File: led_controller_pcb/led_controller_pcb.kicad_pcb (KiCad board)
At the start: 2 copper layers, 50.2 x 99.7 mm, 93 parts, among them J1 DCDC, J10 PASSIVE_OUT, J11 VPP, J12 OUT, J13 VPP, J14 OUT, J15 VPP, J16 PASSIVE_OUT, J17 VPP, J18 OUT, J19 VPP, J2 DEBUG, J20 OUT, J21 LINE1_IN, J22 LINE2_IN, J24 HV_LINE, J25 HV_OUT, J26 HV_LINE, J27 HV_OUT, J28 PSU_LINE1, J29 PSU_LINE2, J3 VPP, J31 PSU_GND, J32 PSU_VOUT, J4 PASSIVE_OUT, J5 VPP, J6 OUT, J7 VPP, J8 OUT, J9 VPP, Q1 IRF540N, Q10 BT136-600, Q2 IRF540N, Q3 IRF540N, Q4 IRF540N, Q5 IRF540N, Q6 IRF540N, Q7 BC549, Q8 BC549, Q9 BT136-600, SW1 BUTTON, SW2 BUTTON, U1 ESP-12E, U2 TC4427A, U3 TC4427A, U4 TC4427A, U5 STM32F030F4Px, U6 MOC3023M, U7 MOC3023M, U8 H11AA1, Y1 8MHz

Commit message: fix tim1 pwm
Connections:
- J2 pad 10: /TX_SCL -> /TX
- J2 pad 8: /RX_SDA -> /RX
- R11 pad 1: /TIM15_CH2 -> /TIM1_CH3
- R7 pad 1: /TIM15_CH1 -> /TIM1_CH2
- U2 pad 2: /TIM15_CH1 -> /TIM1_CH2
- U3 pad 4: /TIM15_CH2 -> /TIM1_CH3
- U5 pad 17: /TX_SCL -> /TIM1_CH2
- U5 pad 18: /RX_SDA -> /TIM1_CH3
- U5 pad 8: /TIM15_CH1 -> /TX
- U5 pad 9: /TIM15_CH2 -> /RX
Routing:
- net /TX: vias 0 -> 2
- net /TIM15_CH1: vias 2 -> 0

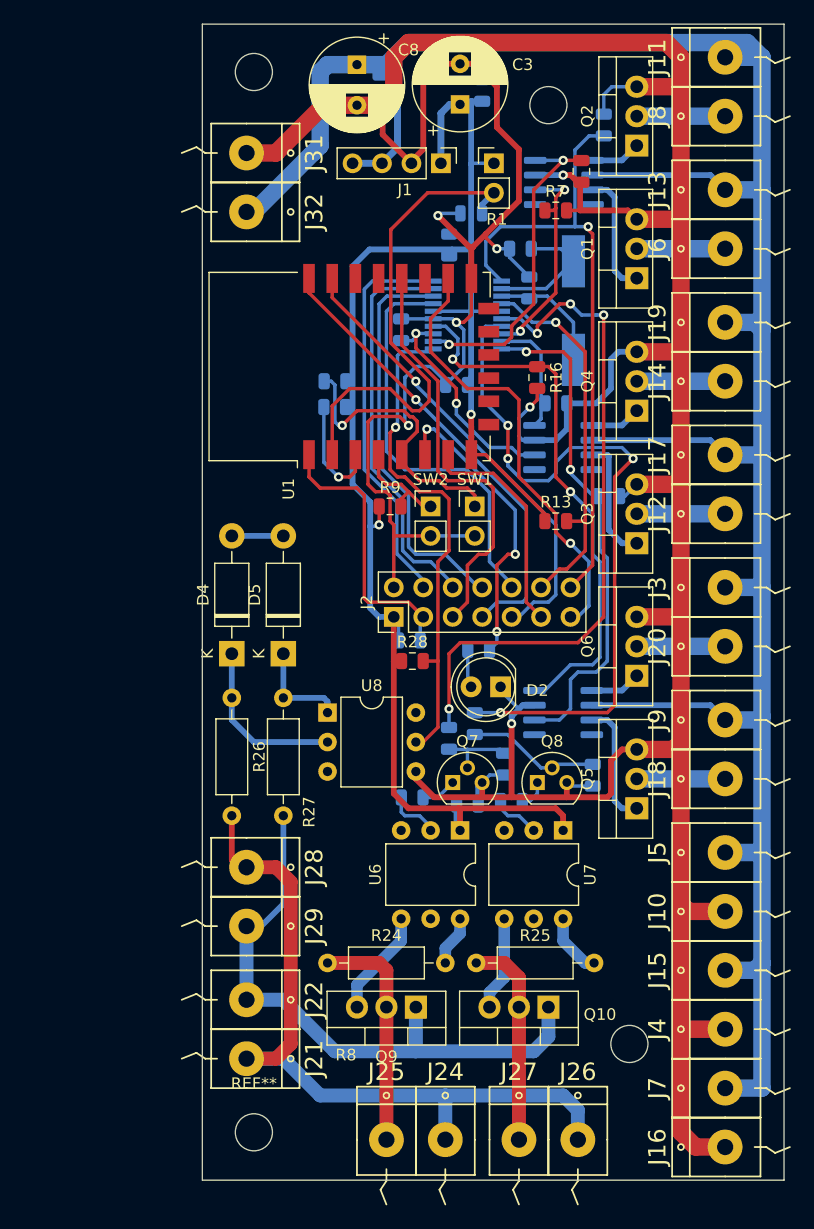
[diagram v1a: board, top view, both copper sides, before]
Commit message: reroute traces to use other timer
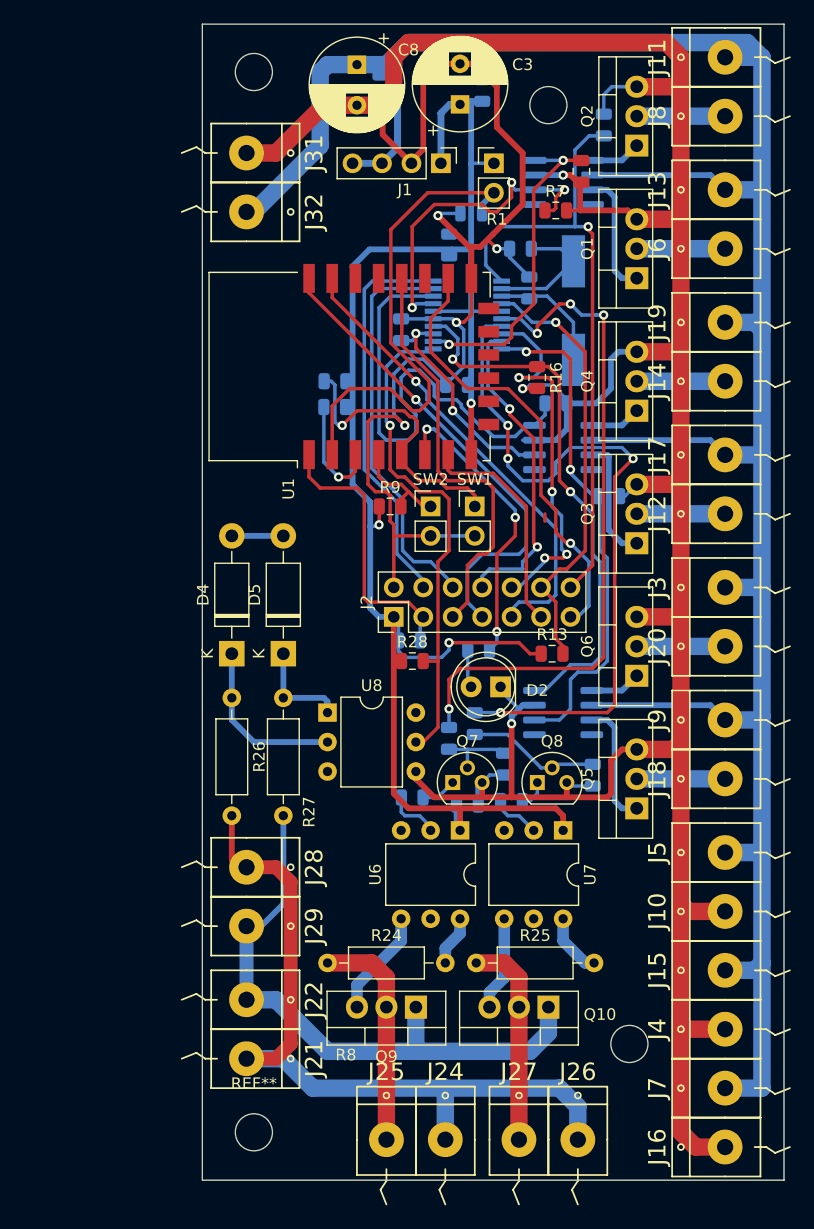
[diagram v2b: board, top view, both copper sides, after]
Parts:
- moved R13 11.4 mm to (147.6, 106.7)
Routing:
- net /TIM1_CH3: track 0.00 -> 42.3 mm
- net /TX_SCL: track 35.7 -> 0.00 mm
- net /RX_SDA: track 34.8 -> 0.00 mm
- net /TX: track 0.00 -> 32.7 mm, vias 2 -> 4
- net /TIM1_CH2: track 0.00 -> 28.4 mm, vias 0 -> 3
- net /RX: track 0.00 -> 28.0 mm, vias 0 -> 2
- net /TIM15_CH1: track 19.1 -> 0.00 mm
- net /TIM15_CH2: track 11.1 -> 0.00 mm
- net +3V3: track 141.4 -> 147.7 mm, vias 2 -> 3
- net /RST: track 32.8 -> 37.7 mm
- net GND: track 368.4 -> 370.9 mm
- net /ESP_TX: track 39.8 -> 41.4 mm
- net /LINE1: track 65.6 -> 66.5 mm
- net /GPO1: track 58.2 -> 58.9 mm
- net /ESP_RX: track 39.9 -> 40.6 mm

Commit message: finalise PCB
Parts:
- added C10: 10p, Capacitor_SMD:C_0805_2012Metric, F.Cu at (135.6, 69.5)
- added R5: 4.7k, Resistor_SMD:R_0805_2012Metric, B.Cu at (137.2, 107.0)
- R13: moved to B.Cu
- moved R9 1.92 mm to (131.7, 94.0)
- moved J2 1.91 mm to (132.1, 103.5)
- moved R3 1.90 mm to (133.4, 105.5)
- moved R13 0.71 mm to (147.0, 106.4)
- moved R28 0.32 mm to (135.9, 107.3)
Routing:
- net /ESP_GP0: track 36.2 -> 40.7 mm
- net /RST: track 37.7 -> 40.2 mm
- net /ESP_RST: track 24.1 -> 21.9 mm
- net GND: track 370.9 -> 373.0 mm
- net /BOOT0: track 55.4 -> 57.3 mm
- net /TIM3_CH4: track 46.8 -> 44.9 mm
- net /SWDIO: track 34.4 -> 32.8 mm
- net Net-(C10-Pad1): track 42.9 -> 41.4 mm
- net /TIM14_CH1: track 43.5 -> 42.1 mm
- net /RX: track 28.0 -> 26.6 mm
- net VDD: track 220.9 -> 219.9 mm
- net /TIM1_CH2: track 28.4 -> 29.3 mm
- net /ESP_RX: track 40.6 -> 39.7 mm
- net Net-(J2-Pad13): track 38.7 -> 37.9 mm
- net /SWCLK: track 34.1 -> 33.3 mm
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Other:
- board size 50.2 x 99.7 mm -> 50 x 99.7 mm
- board text added: "3V3"
- board text added: "EG0"
- board text added: "EN"
- board text added: "ERST"
- board text added: "ERX"
- board text added: "ETX"
- board text added: "G14"
- board text added: "G15"
- board text added: "GND"
- board text added: "SB0"
- board text added: "SRST"
- board text added: "SRX"
- board text added: "STX"
- board text added: "SWC"
- board text added: "SWI"
- board text added: "VI"
- board text added: "VO"
- board text added: "protopit.eu"

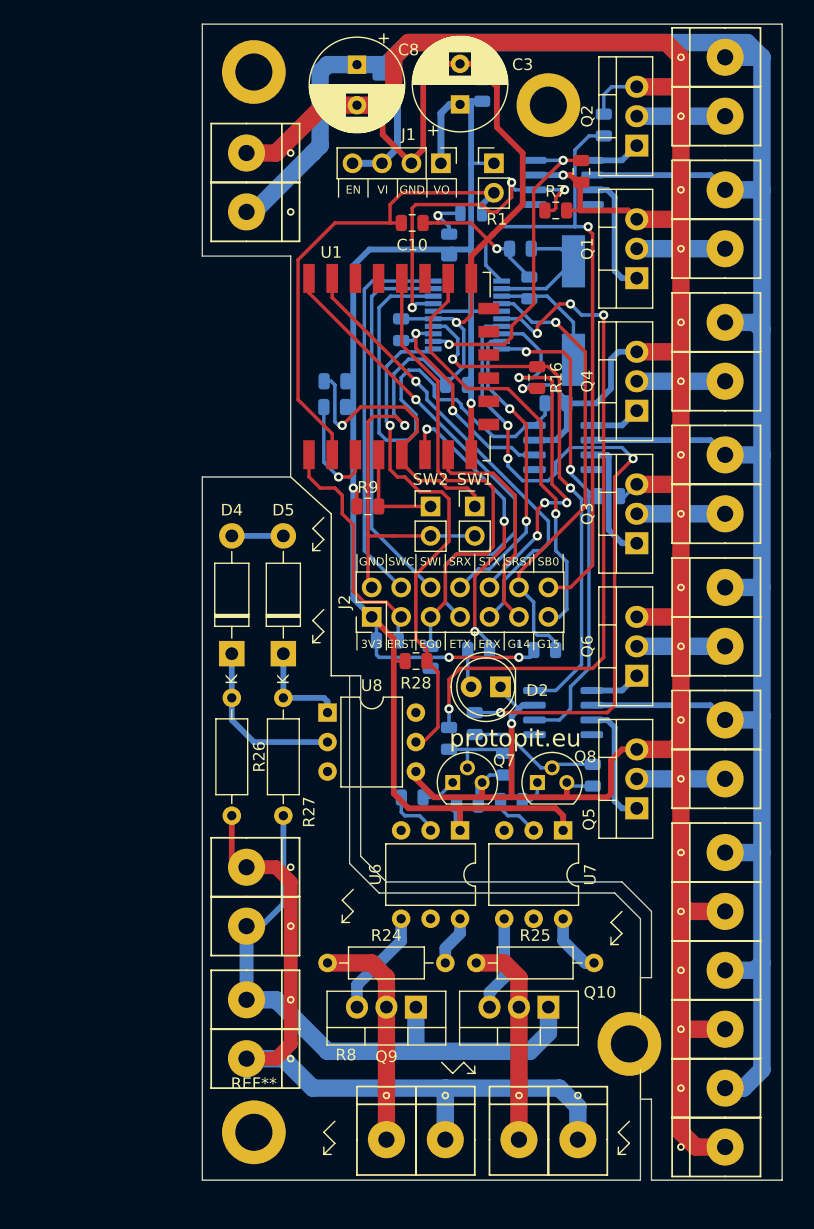
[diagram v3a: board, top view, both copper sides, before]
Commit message: correct size of pcb
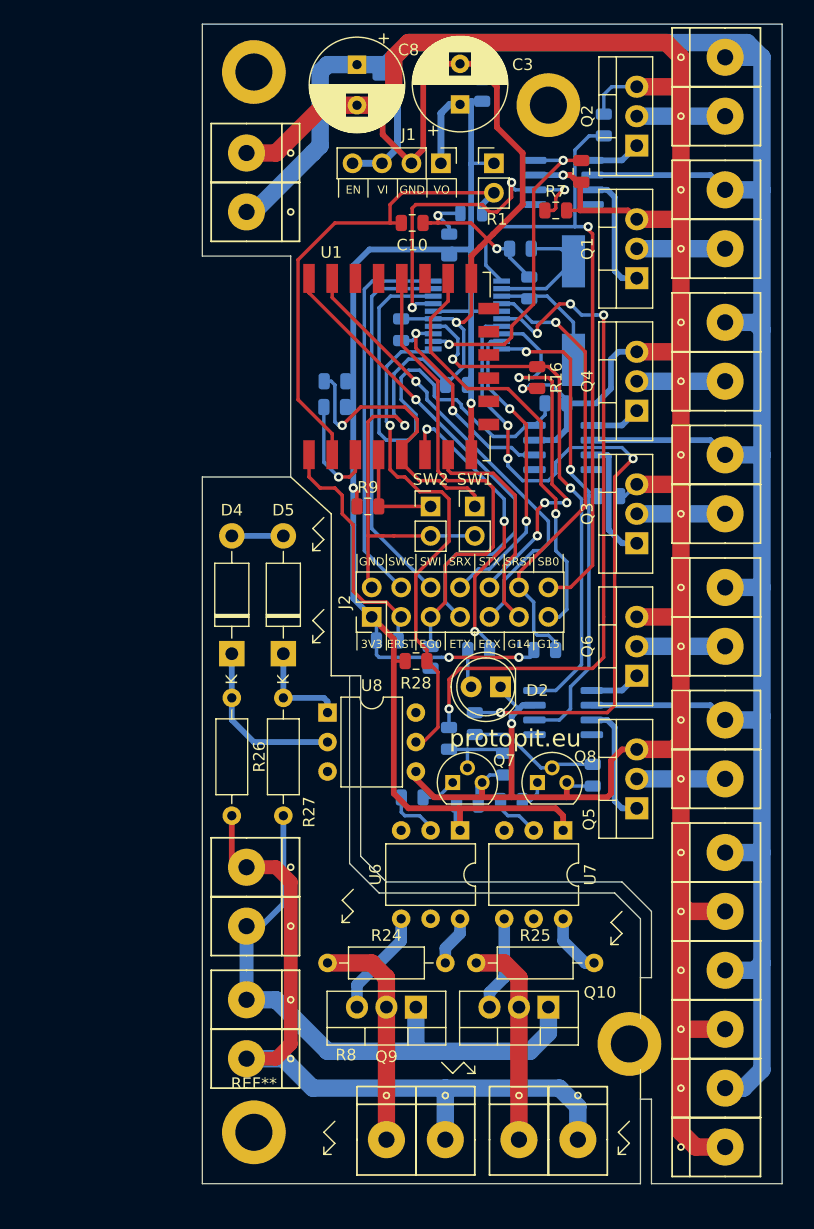
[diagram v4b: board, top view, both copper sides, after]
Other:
- board size 50 x 99.7 mm -> 50 x 100 mm

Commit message: wip on adding a separate connector for high voltage
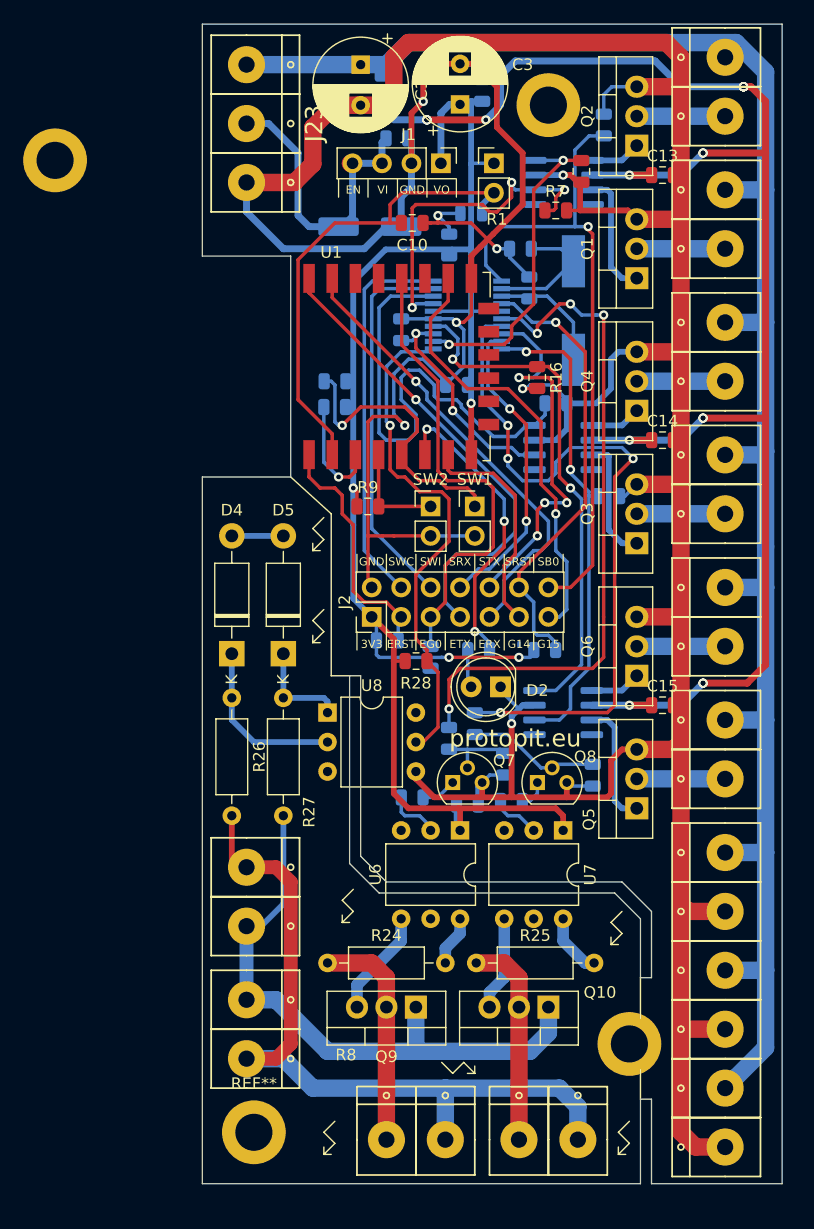
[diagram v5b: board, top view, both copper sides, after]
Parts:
- added C11: 100n, Capacitor_SMD:C_0805_2012Metric, B.Cu at (133.0, 57.8)
- added C12: 470uF, Capacitor_THT:CP_Radial_D8.0mm_P3.50mm, F.Cu at (131.1, 55.9)
- added C13: 100n, Capacitor_SMD:C_0805_2012Metric, F.Cu at (157.2, 65.4)
- added C14: 100n, Capacitor_SMD:C_0805_2012Metric, F.Cu at (157.2, 88.3)
- added C15: 100n, Capacitor_SMD:C_0805_2012Metric, F.Cu at (157.2, 111.1)
- added J23: PSU_VOUT_LOW, connectors:1PIN_DG306, F.Cu at (121.3, 61.0)
- C8: value 470uF -> 220uF; footprint Capacitor_THT:CP_Radial_D8.0mm_P3.50mm -> Capacitor_SMD:CP_Elec_6.3x7.7; moved to B.Cu
- moved REF** 18.8 mm to (104.8, 64.1)
- moved C8 14.0 mm to (131.9, 69.8), turned to 0 degrees
- moved J32 12.7 mm to (121.3, 55.9)
- moved C7 4.75 mm to (134.2, 62.2), turned to 0 degrees
- moved J31 2.54 mm to (121.3, 66.0)
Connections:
- J11 pad 1: VDD -> VPP
- J13 pad 1: VDD -> VPP
- J15 pad 1: VDD -> VPP
- J17 pad 1: VDD -> VPP
- J19 pad 1: VDD -> VPP
- J3 pad 1: VDD -> VPP
- J32 pad 1: VDD -> VPP
- J5 pad 1: VDD -> VPP
- J7 pad 1: VDD -> VPP
- J9 pad 1: VDD -> VPP
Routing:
- net VPP: track 0.00 -> 160.3 mm
- net VDD: track 219.9 -> 165.3 mm, vias 0 -> 18
- net GND: track 373.0 -> 396.0 mm, vias 7 -> 8
- net +3V3: track 147.5 -> 146.6 mm

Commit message: cosmetic fixes
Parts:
- removed C8: 220uF, Capacitor_SMD:CP_Elec_6.3x7.7
- added C16: 220uF, Capacitor_SMD:CP_Elec_6.3x7.7, F.Cu at (140.0, 57.1)
- C13, C14, C15: moved to B.Cu
- C3: footprint Capacitor_THT:CP_Radial_D8.0mm_P3.50mm -> Capacitor_SMD:CP_Elec_6.3x7.7; moved to B.Cu
- J21: value LINE1_IN -> HV_IN_LIVE
- J22: value LINE2_IN -> HV_IN_NEUT
- J28: value PSU_LINE1 -> PSU_LIVE
- J29: value PSU_LINE2 -> PSU_NEUT
- moved REF** 25.3 mm to (129.5, 69.2)
- moved C9 9.42 mm to (136.5, 66.0), turned to 180 degrees
- moved C13 1.85 mm to (158.8, 64.5), turned to 90 degrees
- moved C14 1.85 mm to (158.8, 87.3), turned to 90 degrees
- moved C15 1.85 mm to (158.8, 110.2), turned to 90 degrees
- moved C11 0.98 mm to (133.0, 56.8)
- moved J23 0.95 mm to (121.3, 61.9)
- moved J31 0.95 mm to (121.3, 67.0)
- moved J32 0.95 mm to (121.3, 56.8)
- moved J1 0.72 mm to (137.9, 63.7)
- moved C12 0.71 mm to (130.8, 55.2)
- moved C7 0.65 mm to (134.3, 61.6)
- moved C3 0.33 mm to (140.0, 59.2)
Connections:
- net /LINE1 renamed /LIVE
- net /LINE2 renamed /NEUT
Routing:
- net GND: track 396.0 -> 382.6 mm, vias 8 -> 12
- net +3V3: track 146.6 -> 140.4 mm
- net Net-(C10-Pad1): track 41.4 -> 42.7 mm
- net VPP: track 160.3 -> 160.9 mm
- net VDD: track 165.3 -> 165.7 mm, vias 18 -> 15
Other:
- board text added: "HOUT1"
- board text added: "HOUT2"
- board text added: "LIVE"
- board text added: "NEUT"
- board text added: "OUT1"
- board text added: "OUT2"
- board text added: "OUT3"
- board text added: "OUT4"
- board text added: "OUT5"
- board text added: "OUT6"
- board text added: "VDD"
- board text added: "VPP"

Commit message: some more cosmetic changes
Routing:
- net /LIVE: track 66.5 -> 65.6 mm
- net GND: track 382.6 -> 383.3 mm
- net /ESP_RST: track 21.9 -> 21.3 mm

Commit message: cosmetic changes to led controller pcb
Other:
- board text added: "3v3"
- board text removed: "VI"
- board text removed: "VO"
